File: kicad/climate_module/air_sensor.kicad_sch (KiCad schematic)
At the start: 11 parts, among them U7 ATtiny1614, U8 buffer

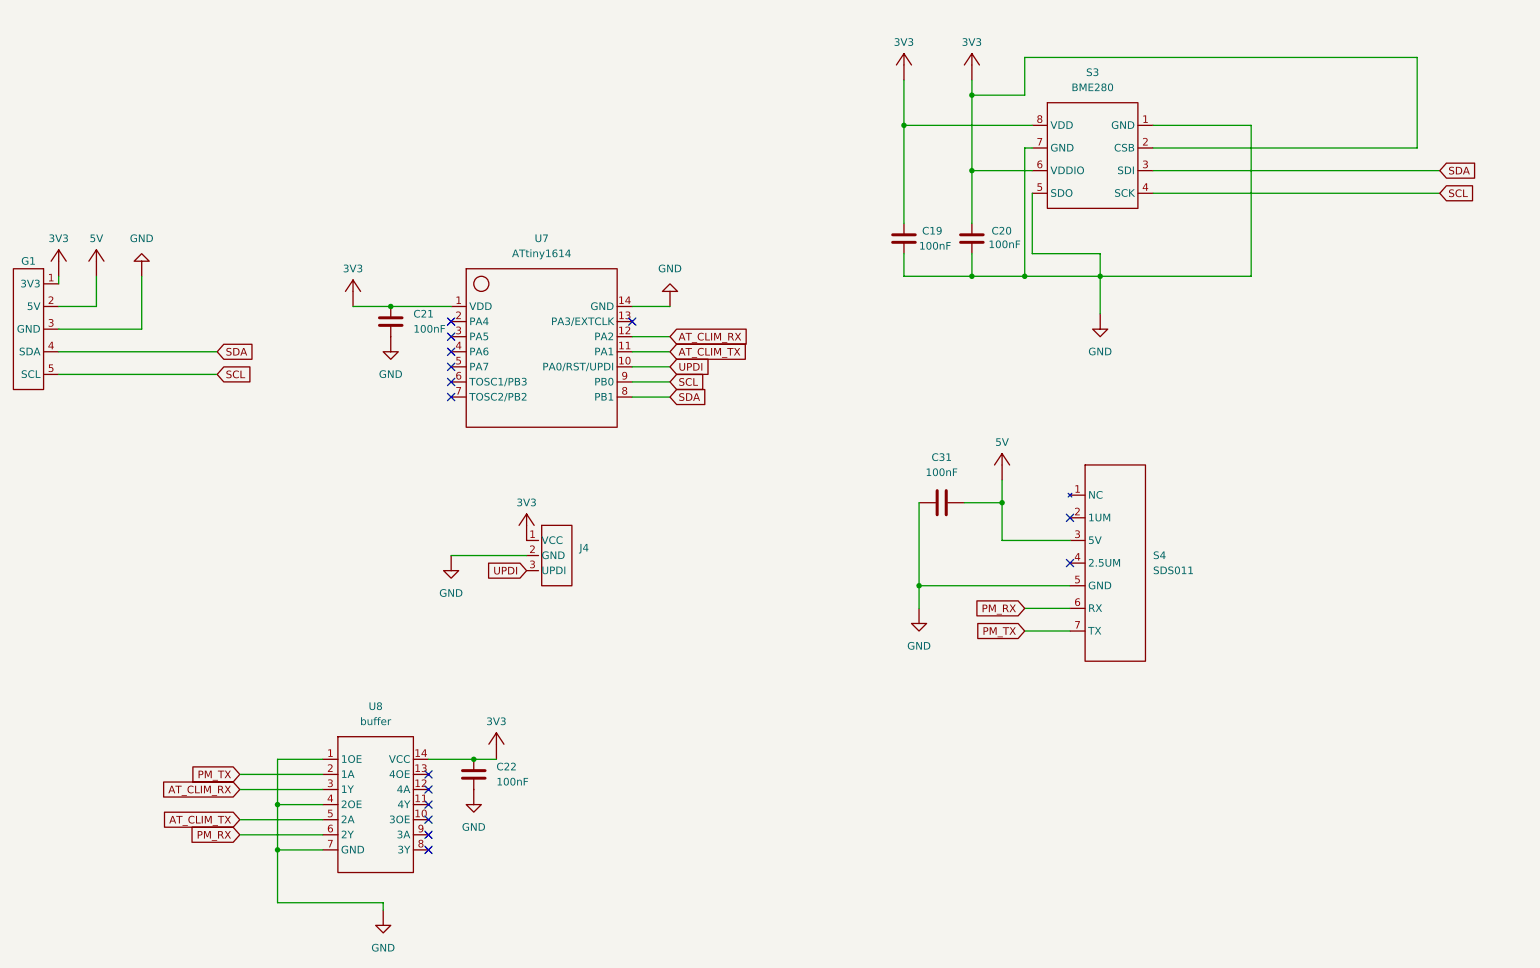
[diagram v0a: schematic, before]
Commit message: added pcb for gas and climate modules
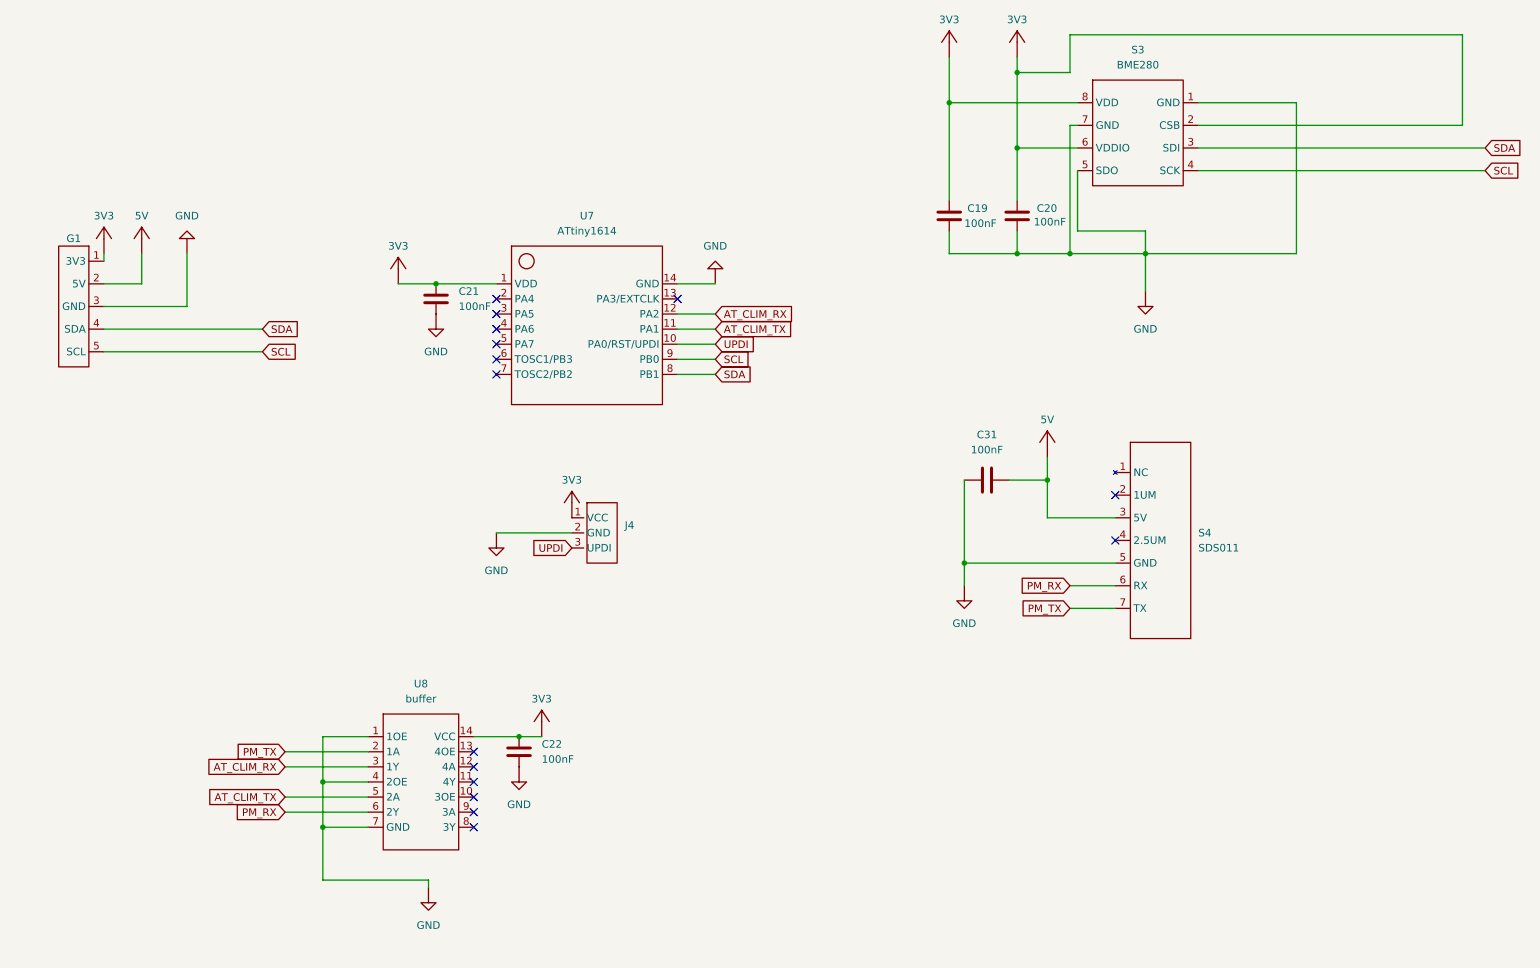
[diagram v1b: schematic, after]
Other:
- moved on the sheet: C19, C20, C21, C22, C31, G1, J4, S3, S4, U7, U8

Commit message: added status LED to climate module
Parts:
- added D1: ~, common:LED_3mm_THT, symbol common:LED
- added R1: 220, common:R_0603, symbol common:Resistor
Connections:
- net GND: now also D1.1 (K)
- net STATUS_LED: now reaches U7.7 (TOSC2/PB2)
- net STATUS_LED: now also R1.1
- new net: D1.2 (A), R1.2
- no-connect marks 15 -> 14
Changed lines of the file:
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@@
-	)
-	(no_connect
-		(at 101.6 86.36)
 	)
 	(no_connect
@@
 		)
 	)
+	(global_label "STATUS_LED"
+		(shape input)
+		(at 238.76 134.62 180)
+		(fields_autoplaced yes)
+		(effects
+			(font
+				(size 1.27 1.27)
+			)
+			(justify right)
+		)
+		(property "Intersheetrefs" "${INTERSHEET_REFS}"
+			(at 224.5868 134.62 0)
+			(effects
+				(font
+					(size 1.27 1.27)
+				)
+				(justify right)
+				(hide yes)
+			)
+		)
+	)
 	(global_label "PM_TX"
 		(shape input)
@@
 		(property "Intersheetrefs" "${INTERSHEET_REFS}"
 			(at 52.532 157.48 0)
+			(effects
+				(font
+					(size 1.27 1.27)
+				)
+				(justify right)
+				(hide yes)
+			)
+		)
+	)
+	(global_label "STATUS_LED"
+		(shape input)
+		(at 101.6 86.36 180)
+		(fields_autoplaced yes)
+		(effects
+			(font
+				(size 1.27 1.27)
+			)
+			(justify right)
+		)
+		(property "Intersheetrefs" "${INTERSHEET_REFS}"
+			(at 87.4268 86.36 0)
 			(effects
 				(font
@@
 	)
 	(symbol
+		(lib_id "common:LED")
+		(at 250.19 134.62 180)
+		(unit 1)
+		(exclude_from_sim no)
+		(in_bom yes)
+		(on_board yes)
+		(dnp no)
+		(fields_autoplaced yes)
+		(property "Reference" "D1"
+			(at 250.445 129.54 0)
+			(effects
+				(font
+					(size 1.27 1.27)
+				)
+			)
+		)
+		(property "Value" "~"
+			(at 250.19 134.62 0)
+			(effects
+				(font
+					(size 1.27 1.27)
+				)
+				(hide yes)
+			)
+		)
+		(property "Footprint" "common:LED_3mm_THT"
+			(at 250.19 134.62 0)
+			(effects
+				(font
+					(size 1.27 1.27)
+				)
+				(hide yes)
+			)
+		)
+		(property "Datasheet" ""
+			(at 250.19 134.62 0)
+			(effects
+				(font
+					(size 1.27 1.27)
+				)
+				(hide yes)
+			)
+		)
+		(property "Description" "Light-Emitting Diode"
+			(at 250.19 130.12 0)
+			(effects
+				(font
+					(size 1.27 1.27)
+				)
+				(hide yes)
+			)
+		)
+		(pin "2"
+		)
+		(pin "1"
+		)
+		(instances
+			(project ""
+				(path "/bd8bb99f-1696-40e4-a829-79b3479834af"
+					(reference "D1")
+					(unit 1)
+				)
+			)
+		)
+	)
+	(symbol
 		(lib_id "common:Capacitor")
 		(at 177.8 59.69 270)
@@
 	)
 	(symbol
+		(lib_id "common:Resistor")
+		(at 242.57 134.62 0)
+		(unit 1)
+		(exclude_from_sim no)
+		(in_bom yes)
+		(on_board yes)
+		(dnp no)
+		(fields_autoplaced yes)
+		(property "Reference" "R1"
+			(at 242.57 129.54 0)
+			(effects
+				(font
+					(size 1.27 1.27)
+				)
+			)
+		)
+		(property "Value" "220"
+			(at 242.57 132.08 0)
+			(effects
+				(font
+					(size 1.27 1.27)
+				)
+			)
+		)
+		(property "Footprint" "common:R_0603"
+			(at 242.57 134.62 0)
+			(effects
+				(font
+					(size 1.27 1.27)
+				)
+				(hide yes)
+			)
+		)
+		(property "Datasheet" ""
+			(at 242.57 134.62 0)
+			(effects
+				(font
+					(size 1.27 1.27)
+				)
+				(hide yes)
+			)
+		)
+		(property "Description" "Resistor"
+			(at 242.57 138.12 0)
+			(effects
+				(font
+					(size 1.27 1.27)
+				)
+				(hide yes)
+			)
+		)
+		(pin "1"
+		)
+		(pin "2"
+		)
+		(instances
+			(project ""
+				(path "/bd8bb99f-1696-40e4-a829-79b3479834af"
+					(reference "R1")
+					(unit 1)
+				)
+			)
+		)
+	)
+	(symbol
 		(lib_id "pwr:GND")
 		(at 180.34 124.46 0)
@@
 					(unit 1)
 				)
+			)
+		)
+	)
+	(symbol
+		(lib_id "pwr:GND")
+		(at 254 137.16 0)
+		(unit 1)
+		(exclude_from_sim no)
+		(in_bom no)
+		(on_board no)
+		(dnp no)
+		(fields_autoplaced yes)
+		(property "Reference" "#GND01"
+			(at 254 124.16 0)
+			(effects
+				(font
+					(size 1.27 1.27)
+				)
+				(hide yes)
+			)
+		)
+		(property "Value" "GND"
+			(at 254 140.97 0)
+			(effects
+				(font
+					(size 1.27 1.27)
+				)
+			)
+		)
+		(property "Footprint" ""
+			(at 254 137.16 0)
+			(effects
+				(font
+					(size 1.27 1.27)
+				)
+				(hide yes)
+			)
+		)
+		(property "Datasheet" ""
+			(at 254 137.16 0)
+			(effects
+				(font
+					(size 1.27 1.27)
+				)
+				(hide yes)
+			)
+		)
+		(property "Description" "Ground"
+			(at 254 141.66 0)
+			(effects
+				(font
+					(size 1.27 1.27)
+				)
+				(hide yes)
+			)
+		)
+		(pin "1"
+		)
+		(instances
+			(project ""
+				(path "/bd8bb99f-1696-40e4-a829-79b3479834af"
+					(reference "#GND01")
+					(unit 1)
+				)
